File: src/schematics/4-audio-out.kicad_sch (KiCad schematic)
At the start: 2 parts

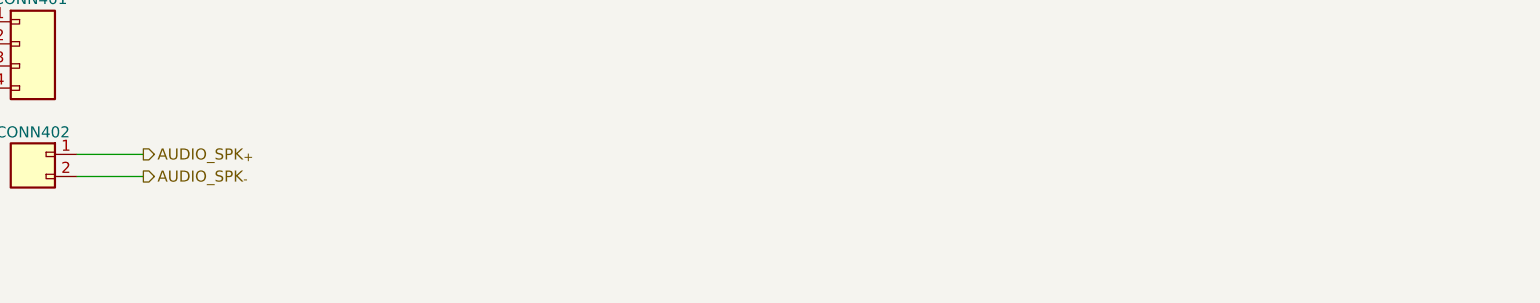
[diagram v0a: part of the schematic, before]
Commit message: Further MCU elaboration and pin mapping.
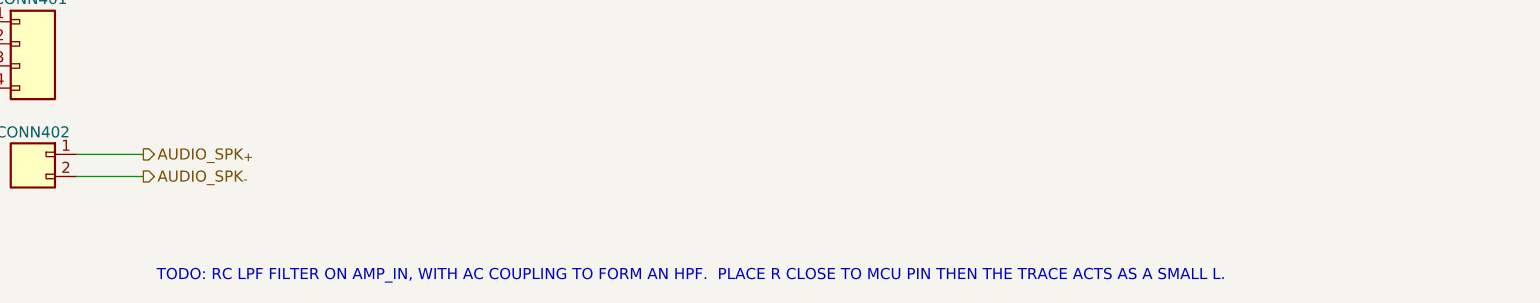
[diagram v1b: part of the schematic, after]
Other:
- note added: "TODO: RC LPF FILTER ON AMP_IN, WITH AC COUPLING TO FORM AN HPF. PLACE R CLOSE TO MCU PIN THEN THE TRACE ACTS AS A SMALL L."
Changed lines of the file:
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@@
     (stroke (width 0) (type default))
+  )
+  (text "TODO: RC LPF FILTER ON AMP_IN, WITH AC COUPLING TO FORM AN HPF.  PLACE R CLOSE TO MCU PIN THEN THE TRACE ACTS AS A SMALL L."
+    (at 115.824 89.662 0)
+    (effects (font (size 1.27 1.27)) (justify left bottom))
   )
   (label "AMP_EN" (at 88.9 64.77 0) (fields_autoplaced)

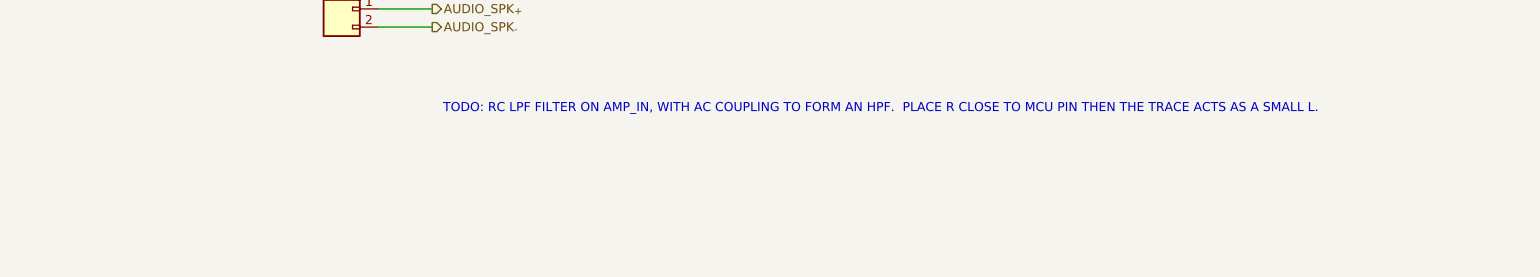
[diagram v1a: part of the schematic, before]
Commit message: Further elaboration of the design and schematics, mainly power supply calculations.
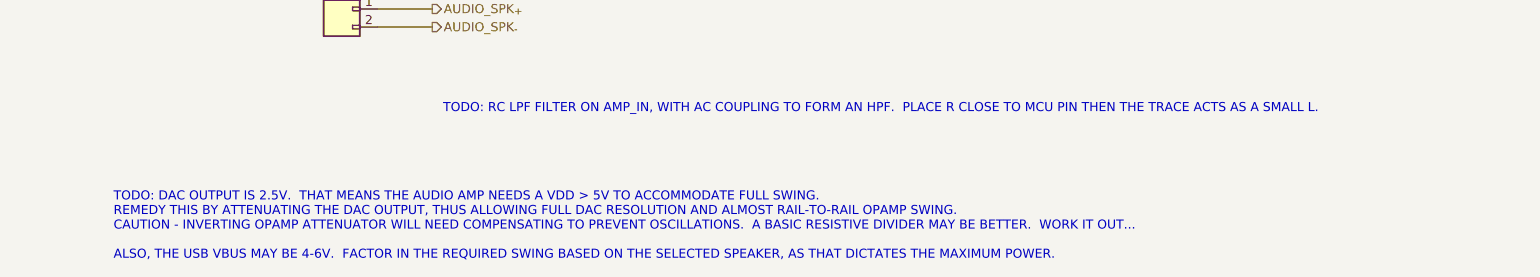
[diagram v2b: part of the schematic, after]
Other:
- note added: "TODO: DAC OUTPUT IS 2.5V. THAT MEANS THE AUDIO AMP NEEDS A VDD > 5V TO ACCOMMODATE FULL SWING. REMEDY THIS BY ATTENUATING THE DAC OUTPUT, THUS ALLOWING FULL DAC RESOLUTION AND ALMOST RAIL-TO-RAIL OPAMP SWING. CAUTION - INVERTING OPAMP ATTENUATOR WILL NEED COMPENSATING TO PREVENT OSCILLATIONS. A BASIC RESISTIVE DIVIDER MAY BE BETTER. WORK IT OUT... ALSO, THE USB VBUS MAY BE 4-6V. FACTOR IN THE REQ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"
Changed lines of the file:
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@@
+    (effects (font (size 1.27 1.27)) (justify left bottom))
+  )
+  (text "TODO: DAC OUTPUT IS 2.5V.  THAT MEANS THE AUDIO AMP NEEDS A VDD > 5V TO ACCOMMODATE FULL SWING.\nREMEDY THIS BY ATTENUATING THE DAC OUTPUT, THUS ALLOWING FULL DAC RESOLUTION AND ALMOST RAIL-TO-RAIL OPAMP SWING.\nCAUTION - INVERTING OPAMP ATTENUATOR WILL NEED COMPENSATING TO PREVENT OSCILLATIONS.  A BASIC RESISTIVE DIVIDER MAY BE BETTER.  WORK IT OUT...\n\nALSO, THE USB VBUS MAY BE 4-6V.  FACTOR IN THE REQUIRED SWING BASED ON THE SELECTED SPEAKER, AS THAT DICTATES THE MAXIMUM POWER."
+    (at 69.596 110.236 0)
     (effects (font (size 1.27 1.27)) (justify left bottom))
   )

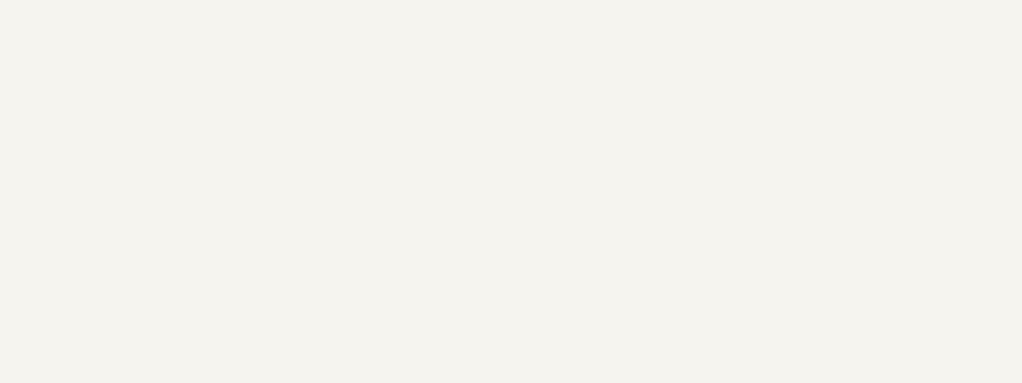
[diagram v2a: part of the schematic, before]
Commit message: Further elaboration of the USB / Power schematic.
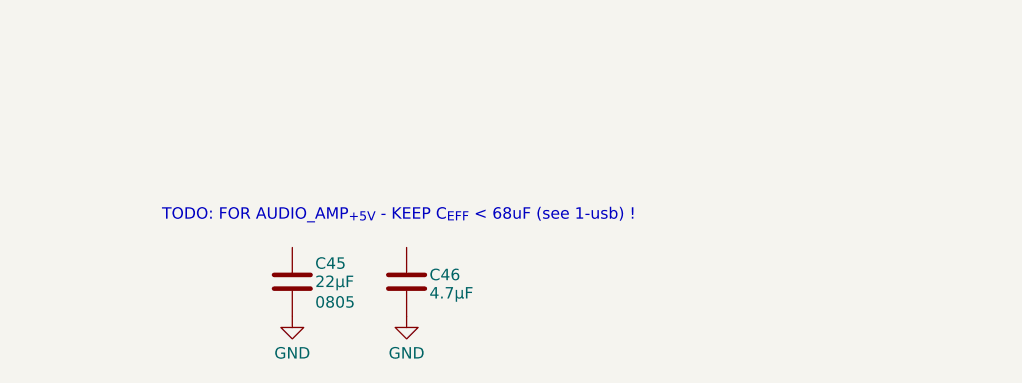
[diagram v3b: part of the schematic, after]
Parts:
- added C45: 22μF, restall-generic-capacitors:unpolarised-nominal-0805-2012, symbol restall-generic-capacitors:capacitor-unpolarised
- added C46: 4.7μF, restall-generic-capacitors:unpolarised-nominal-0402-1005, symbol restall-generic-capacitors:capacitor-unpolarised
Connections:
- new net GND: C45.2, C46.2
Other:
- note added: "TODO: FOR AUDIO_AMP_{+5V} - KEEP C_{EFF} < 68uF (see 1-usb) !"
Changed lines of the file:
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@@
     (stroke (width 0) (type default))
+  )
+  (text "TODO: FOR AUDIO_AMP_{+5V} - KEEP C_{EFF} < 68uF (see 1-usb) !"
+    (at 137.922 149.606 0)
+    (effects (font (size 1.27 1.27)) (justify left bottom))
   )
   (text "TODO: RC LPF FILTER ON AMP_IN, WITH AC COUPLING TO FORM AN HPF.  PLACE R CLOSE TO MCU PIN THEN THE TRACE ACTS AS A SMALL L."
@@
     (effects (font (size 1.27 1.27)) (justify right))
   )
+  (symbol (lib_id "restall-generic-power:GND") (at 165.1 160.02 0) (unit 1)
+    (in_bom yes) (on_board yes) (dnp no) (fields_autoplaced)
+    (property "Reference" "#PWR0100" (at 165.1 166.37 0)
+      (effects (font (size 1.27 1.27)) hide)
+    )
+    (property "Value" "GND" (at 165.1 164.1531 0)
+      (effects (font (size 1.27 1.27)))
+    )
+    (property "Footprint" "" (at 165.1 160.02 0)
+      (effects (font (size 1.27 1.27)) hide)
+    )
+    (property "Datasheet" "" (at 165.1 160.02 0)
+      (effects (font (size 1.27 1.27)) hide)
+    )
+    (pin "1")
+    (instances
+      (project "msf-owl-clock"
+        (path "/56d623d3-22db-4d43-a9d9-e6bb4bb68946/6f5a1439-79e4-455f-9974-b67d6790034b"
+          (reference "#PWR0100") (unit 1)
+        )
+      )
+    )
+  )
   (symbol (lib_id "restall-generic-connectors:header-1x4") (at 101.6 63.5 0) (unit 1)
     (in_bom yes) (on_board yes) (dnp no)
@@
         (path "/56d623d3-22db-4d43-a9d9-e6bb4bb68946/6f5a1439-79e4-455f-9974-b67d6790034b"
           (reference "CONN401") (unit 1)
+        )
+      )
+    )
+  )
+  (symbol (lib_id "restall-generic-power:GND") (at 152.4 160.02 0) (unit 1)
+    (in_bom yes) (on_board yes) (dnp no) (fields_autoplaced)
+    (property "Reference" "#PWR099" (at 152.4 166.37 0)
+      (effects (font (size 1.27 1.27)) hide)
+    )
+    (property "Value" "GND" (at 152.4 164.1531 0)
+      (effects (font (size 1.27 1.27)))
+    )
+    (property "Footprint" "" (at 152.4 160.02 0)
+      (effects (font (size 1.27 1.27)) hide)
+    )
+    (property "Datasheet" "" (at 152.4 160.02 0)
+      (effects (font (size 1.27 1.27)) hide)
+    )
+    (pin "1")
+    (instances
+      (project "msf-owl-clock"
+        (path "/56d623d3-22db-4d43-a9d9-e6bb4bb68946/6f5a1439-79e4-455f-9974-b67d6790034b"
+          (reference "#PWR099") (unit 1)
         )
       )
@@
         )
       )
+    )
+  )
+  (symbol (lib_id "restall-generic-capacitors:capacitor-unpolarised") (at 152.4 156.21 0) (unit 1)
+    (in_bom yes) (on_board yes) (dnp no)
+    (property "Reference" "C45" (at 154.94 154.178 0)
+      (effects (font (size 1.27 1.27)) (justify left))
+    )
+    (property "Value" "22μF" (at 154.94 156.21 0)
+      (effects (font (size 1.27 1.27)) (justify left))
+    )
+    (property "Footprint" "restall-generic-capacitors:unpolarised-nominal-0805-2012" (at 155.702 169.926 0)
+      (effects (font (size 1.27 1.27)) (justify left) hide)
+    )
+    (property "Datasheet" "https://product.samsungsem.com/mlcc/CL21A226MPQNNN.do" (at 152.4 156.21 0)
+      (effects (font (size 1.27 1.27)) (justify left) hide)
+    )
+    (property "Label" "22μF±20% 10V X5R" (at 155.702 157.734 0)
+      (effects (font (size 1.27 1.27)) (justify left) hide)
+    )
+    (property "Tolerance" "±20%" (at 155.702 159.766 0)
+      (effects (font (size 1.27 1.27)) (justify left) hide)
+    )
+    (property "VoltageRating" "10V" (at 155.702 161.798 0)
+      (effects (font (size 1.27 1.27)) (justify left) hide)
+    )
+    (property "TemperatureCoefficient" "X5R" (at 155.702 163.83 0)
+      (effects (font (size 1.27 1.27)) (justify left) hide)
+    )
+    (property "Dielectric" "MLCC" (at 155.702 165.862 0)
+      (effects (font (size 1.27 1.27)) (justify left) hide)
+    )
+    (property "Package" "0805" (at 154.94 158.496 0)
+      (effects (font (size 1.27 1.27)) (justify left))
+    )
+    (property "Manufacturer" "Samsung" (at 152.4 156.21 0)
+      (effects (font (size 1.27 1.27)) (justify left) hide)
+    )
+    (property "ManufacturerPartNumber" "CL21A226MPQNNN" (at 152.4 156.21 0)
+      (effects (font (size 1.27 1.27)) (justify left) hide)
+    )
+    (property "Manufacturer2" "" (at 152.4 156.21 0)
+      (effects (font (size 1.27 1.27)) (justify left) hide)
+    )
+    (property "Manufacturer2PartNumber" "" (at 152.4 156.21 0)
+      (effects (font (size 1.27 1.27)) (justify left) hide)
+    )
+    (pin "1")
+    (pin "2")
+    (instances
+      (project "msf-owl-clock"
+        (path "/56d623d3-22db-4d43-a9d9-e6bb4bb68946/6f5a1439-79e4-455f-9974-b67d6790034b"
+          (reference "C45") (unit 1)
+        )
+      )
+    )
+  )
+  (symbol (lib_id "restall-generic-capacitors:capacitor-unpolarised") (at 165.1 156.21 0) (unit 1)
+    (in_bom yes) (on_board yes) (dnp no)
+    (property "Reference" "C46" (at 167.64 155.448 0)
+      (effects (font (size 1.27 1.27)) (justify left))
+    )
+    (property "Value" "4.7μF" (at 167.64 157.48 0)
+      (effects (font (size 1.27 1.27)) (justify left))
+    )
+    (property "Footprint" "restall-generic-capacitors:unpolarised-nominal-0402-1005" (at 168.402 169.926 0)
+      (effects (font (size 1.27 1.27)) (justify left) hide)
+    )
+    (property "Datasheet" "" (at 165.1 156.21 0)
+      (effects (font (size 1.27 1.27)) (justify left) hide)
+    )
+    (property "Label" "4.7μF±20% 10V X5R" (at 168.402 157.734 0)
+      (effects (font (size 1.27 1.27)) (justify left) hide)
+    )
+    (property "Tolerance" "±20%" (at 168.402 159.766 0)
+      (effects (font (size 1.27 1.27)) (justify left) hide)
+    )
+    (property "VoltageRating" "10V" (at 167.64 157.48 0)
+      (effects (font (size 1.27 1.27)) (justify left) hide)
+    )
+    (property "TemperatureCoefficient" "X5R" (at 168.402 163.83 0)
+      (effects (font (size 1.27 1.27)) (justify left) hide)
+    )
+    (property "Dielectric" "MLCC" (at 168.402 165.862 0)
+      (effects (font (size 1.27 1.27)) (justify left) hide)
+    )
+    (property "Package" "0402" (at 167.64 158.242 0)
+      (effects (font (size 1.27 1.27)) (justify left) hide)
+    )
+    (property "Manufacturer" "Samsung" (at 165.1 156.21 0)
+      (effects (font (size 1.27 1.27)) (justify left) hide)
+    )
+    (property "ManufacturerPartNumber" "" (at 165.1 156.21 0)
+      (effects (font (size 1.27 1.27)) (justify left) hide)
+    )
+    (property "Manufacturer2" "" (at 165.1 156.21 0)
+      (effects (font (size 1.27 1.27)) (justify left) hide)
+    )
+    (property "Manufacturer2PartNumber" "" (at 165.1 156.21 0)
+      (effects (font (size 1.27 1.27)) (justify left) hide)
+    )
+    (pin "1")
+    (pin "2")
+    (instances
+      (project "msf-owl-clock"
+        (path "/56d623d3-22db-4d43-a9d9-e6bb4bb68946/6f5a1439-79e4-455f-9974-b67d6790034b"
+          (reference "C46") (unit 1)
+        )
+      )

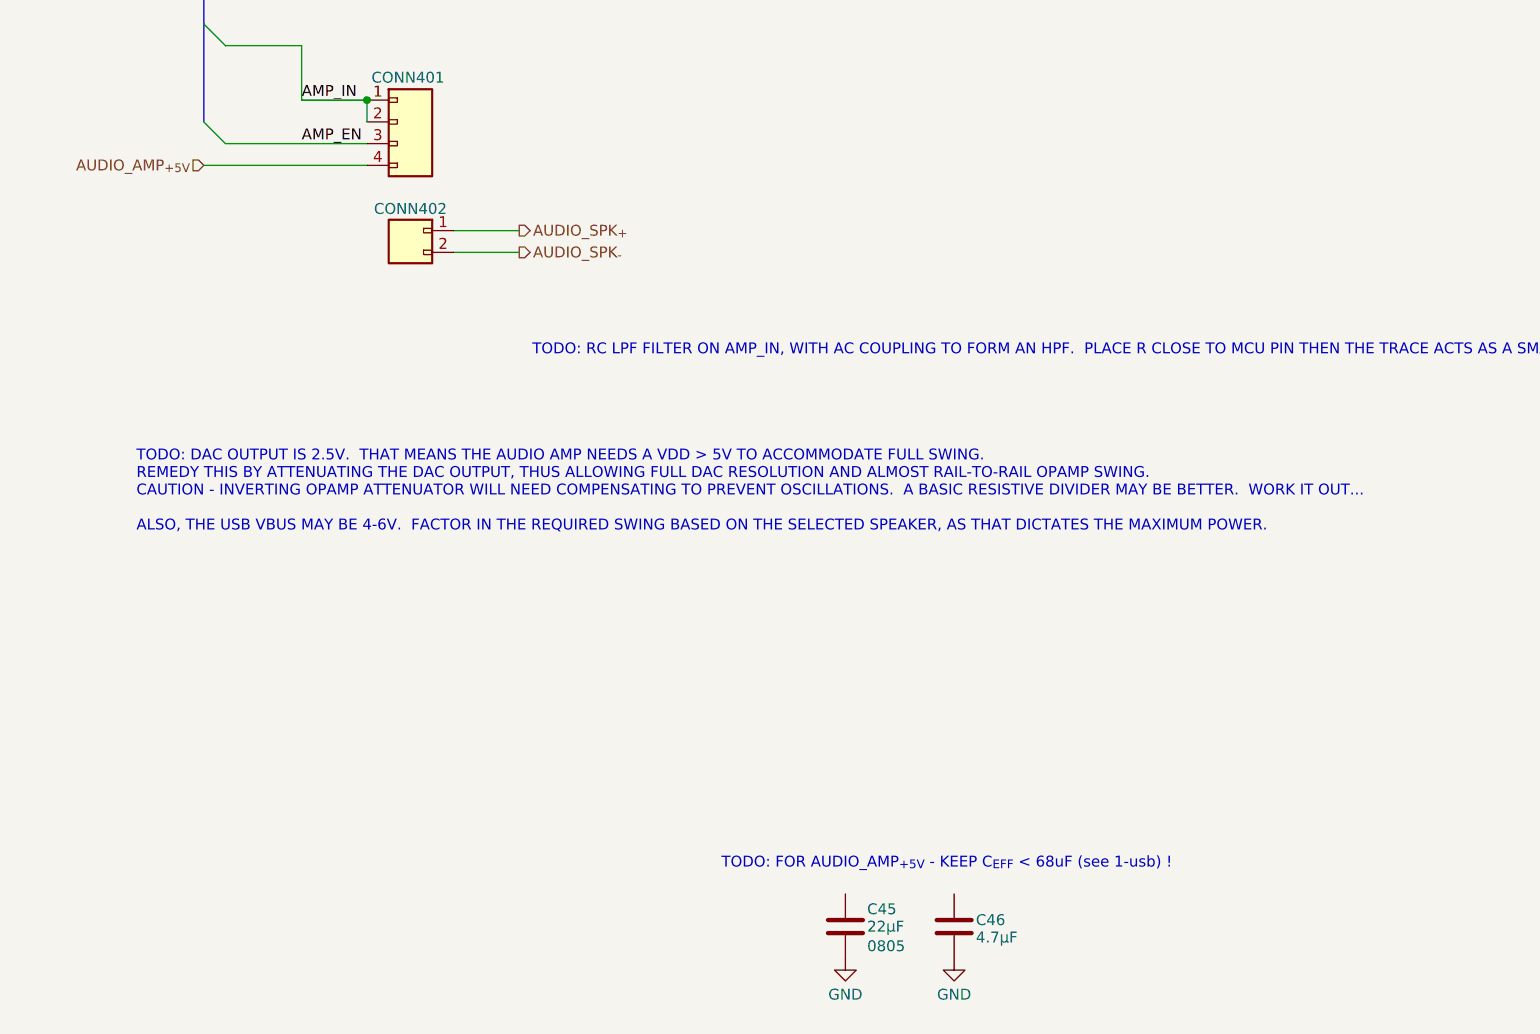
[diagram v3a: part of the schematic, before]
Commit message: Further elaboration of the USB / power module schematics.
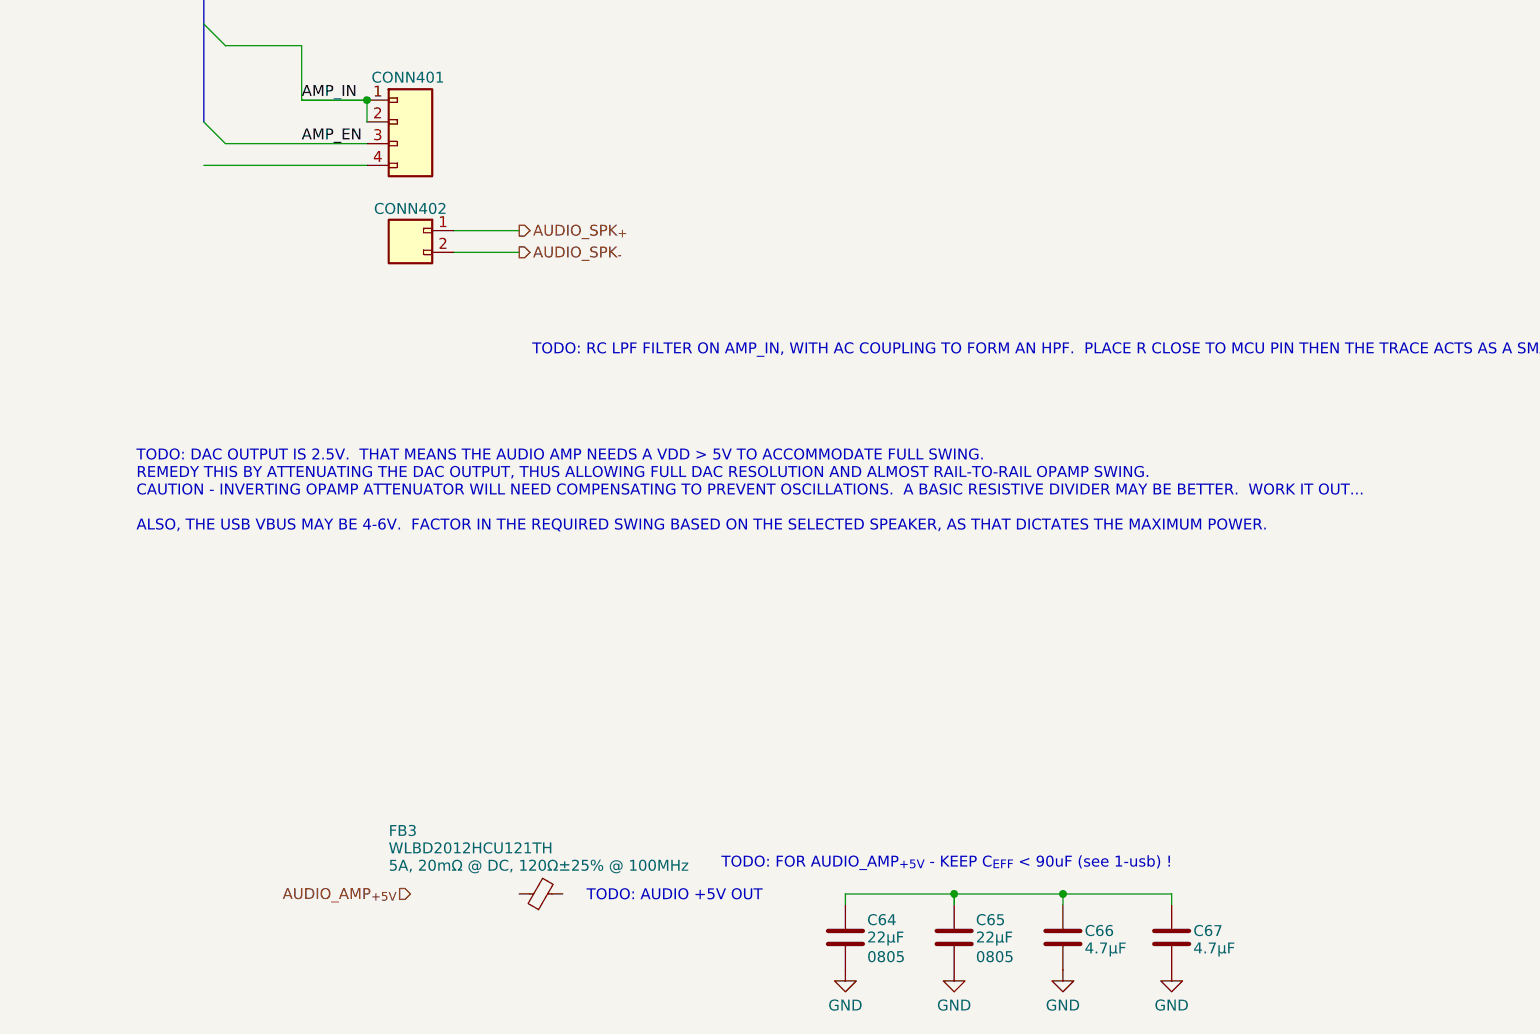
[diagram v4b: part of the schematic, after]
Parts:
- removed C45: 22μF, restall-generic-capacitors:unpolarised-nominal-0805-2012, symbol restall-generic-capacitors:capacitor-unpolarised
- removed C46: 4.7μF, restall-generic-capacitors:unpolarised-nominal-0402-1005, symbol restall-generic-capacitors:capacitor-unpolarised
- added C64, C65: 22μF, restall-generic-capacitors:unpolarised-nominal-0805-2012, symbol restall-generic-capacitors:capacitor-unpolarised
- added C66, C67: 4.7μF, restall-generic-capacitors:unpolarised-nominal-0402-1005, symbol restall-generic-capacitors:capacitor-unpolarised
- added FB3: WLBD2012HCU121TH, restall-manufacturer-walsin:WLBD2012, symbol restall-manufacturer-walsin:WLBD2012HCU121TH
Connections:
- net AUDIO_AMP_{+5V}: no longer CONN401.4 (P4)
- net GND: now also C64.2, C65.2, C66.2, C67.2
- new net: C64.1, C65.1, C66.1, C67.1
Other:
- note added: "TODO: AUDIO +5V OUT"
- note added: "TODO: FOR AUDIO_AMP_{+5V} - KEEP C_{EFF} < 90uF (see 1-usb) !"
- note removed: "TODO: FOR AUDIO_AMP_{+5V} - KEEP C_{EFF} < 68uF (see 1-usb) !"
